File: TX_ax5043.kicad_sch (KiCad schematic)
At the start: 29 parts, among them P6 CONUFL001-SMD-T, P7 CONUFL001-SMD-T, Q7 DMP2160UWQ-7, U23 AX5043

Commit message: Add licensing
Use CERN-OHL-W version 2

Signed-off-by: Corey Minyard <corey@minyard.net>
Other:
- note removed: "TRANSMITTER"
- title: Radiation Tolerant PacSat Communication -> AX5043 Transmitter
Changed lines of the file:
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@@
 	(paper "USLedger")
 	(title_block
-		(title "Radiation Tolerant PacSat Communication")
-		(date "2023-06-17")
-		(rev "A")
+		(title "AX5043 Transmitter")
+		(date "2026-08-20")
+		(rev "4.0")
 		(company "AMSAT-NA")
-		(comment 1 "N5BRG")
+		(comment 1 "AE5KM")
+		(comment 2 "Copyright Corey Minyard, 2026")
+		(comment 3 "Licensed under CERN-OHL-W version 2")
 	)
 	(text "TX_DRV"
@@
 			)
 			(justify left bottom)
-		)
-	)
-	(text "TRANSMITTER"
-		(exclude_from_sim no)
-		(at 317.5 245.11 0)
-		(effects
-			(font
-				(size 6.35 6.35)
-			)
-			(justify left bottom)

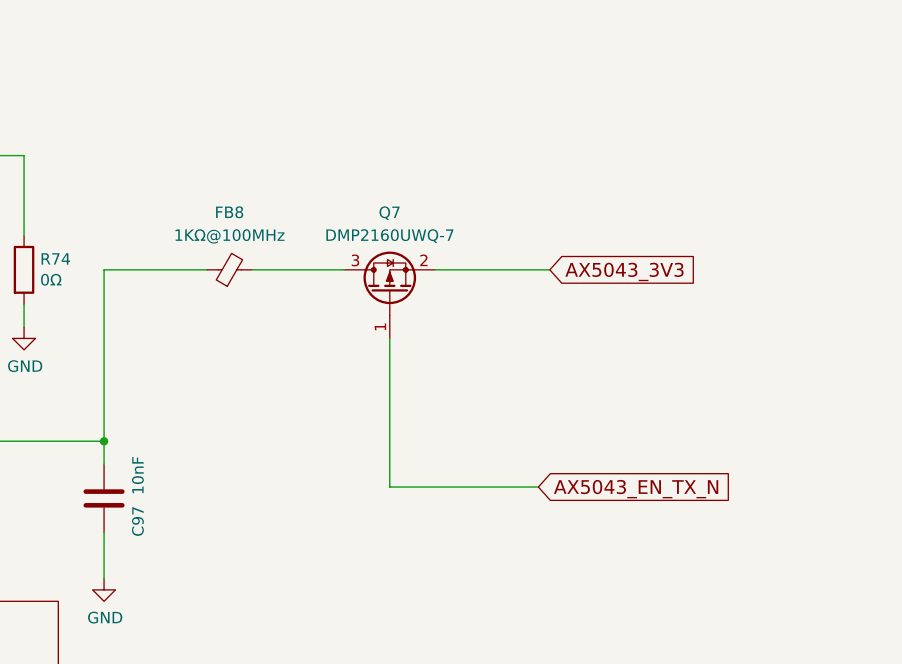
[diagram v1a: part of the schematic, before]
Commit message: Cost reduce the AX5043 power control
Change the MOSFET + ferrite bead combo on all the AX5043 power inputs
to a inrush-controlled power controller.  The space-rated ferrites are
just too expensive.

Signed-off-by: Corey Minyard <corey@minyard.net>
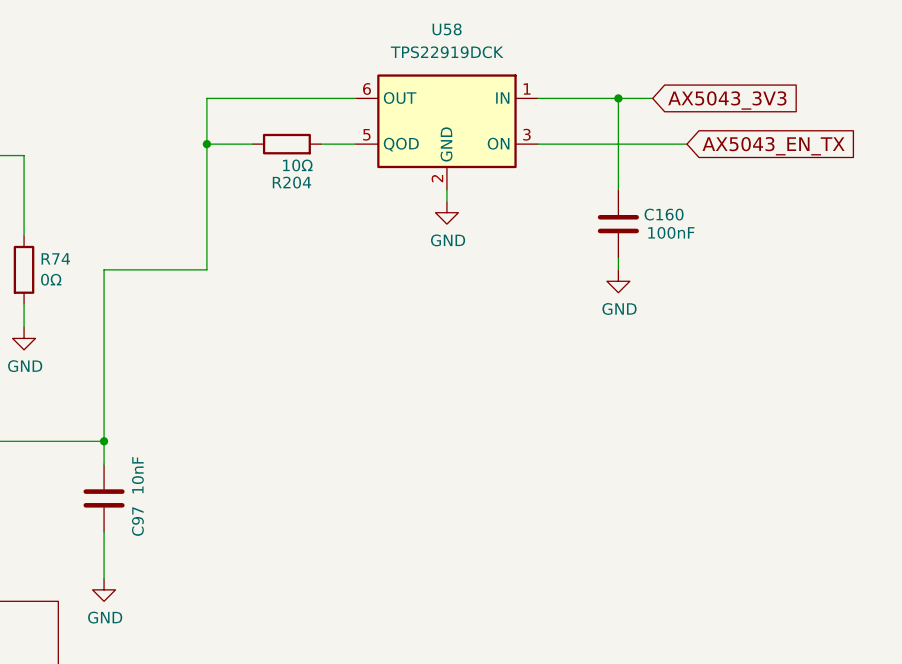
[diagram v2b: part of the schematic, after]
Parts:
- removed FB8: 1KΩ@100MHz, Inductor_SMD:L_0603_1608Metric_Pad1.05x0.95mm_HandSolder, symbol Device:FerriteBead_Small
- removed Q7: DMP2160UWQ-7, Package_TO_SOT_SMD:SOT-323_SC-70, symbol Transistor_FET:Q_PMOS_GSD
- added C160: 100nF, Capacitor_SMD:C_0402_1005Metric_Pad0.74x0.62mm_HandSolder, symbol Device:C
- added R204: 10Ω, Resistor_SMD:R_0402_1005Metric_Pad0.72x0.64mm_HandSolder, symbol Device:R
- added U58: TPS22919DCK, Package_TO_SOT_SMD:SOT-363_SC-70-6, symbol Power_Management:TPS22919DCK
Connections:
- net AX5043_3V3: now also C160.1, U58.1 (IN)
- net GND: now also C160.2, U58.2 (GND)
- net at C97.1, U23.23 (VDD_IO): now also R204.1, U58.6 (OUT)
- new net: R204.2, U58.5 (QOD)
- new net AX5043_EN_TX: U58.3 (ON)
